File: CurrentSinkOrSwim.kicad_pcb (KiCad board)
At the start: 2 copper layers, 41.6 x 50.5 mm, 23 parts, among them P101 CONN_01X02, P102 CONN_01X03, P103 CONN_01X02, P201 CONN_01X01, Q201 BUK9575, U201 LMV358, U401 LM2931

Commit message: Lets try layout one more time. Starting layout from scratch
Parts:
- C201, C301, C401, C402: moved to F.Cu
- moved P101 74.4 mm to (184.3, 86.9), turned to 0 degrees
- moved C401 65.2 mm to (180.9, 111.4)
- moved R402 65.0 mm to (176.7, 111.4)
- moved C402 63.9 mm to (185.5, 105.2)
- moved R401 61.0 mm to (176.7, 105.2)
- moved RV301 59.0 mm to (106.1, 127.0), turned to 0 degrees
- moved P103 55.8 mm to (195.9, 86.9), turned to 0 degrees
- moved R403 54.3 mm to (181.1, 105.2)
- moved D301 52.7 mm to (117.9, 124.0), turned to 0 degrees
- moved P102 51.8 mm to (173.4, 85.4), turned to 0 degrees
- moved U401 51.0 mm to (171.5, 106.1), turned to 0 degrees
- moved R302 46.6 mm to (118.8, 132.0)
- moved Q201 45.8 mm to (123.3, 110.8)
- moved C301 45.7 mm to (114.5, 132.0)
- moved RV201 40.5 mm to (148.2, 87.0), turned to 0 degrees
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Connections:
- P102 pad 3: Net-(P102-Pad3) -> /Current Control/Current_Sink+
- P103 pad 1: Net-(P102-Pad3) -> /Current Control/Current_Sink+
- Q201 pad 1: /Current Control/Current_Sink+ -> /Current Control/FetGate
- Q201 pad 2: /Current Control/FetGate -> /Current Control/Current_Sink+
- R203 pad 2: /Current Control/Current_Sink- -> GND
- R302 pad 1: /Voltage Control/Current_Sink+ -> /Current Control/Current_Sink+
- RV201 pad 2: /Current Control/Current_Sink- -> GND
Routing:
- removed copper zone on B.Cu, net GND
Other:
- board outline removed
- rule pad_to_mask_clearance: 0.2 -> 0

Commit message: Intermediate layout version 2
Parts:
- C201, C301, C401, C402: moved to B.Cu
- moved R203 74.1 mm to (163.2, 68.8)
- moved D301 74.0 mm to (159.5, 62.8), turned to 180 degrees
- moved R302 72.3 mm to (152.1, 67.9), turned to 270 degrees
- moved Q201 65.0 mm to (159.5, 56.8)
- moved R301 60.5 mm to (145.3, 71.3), turned to 90 degrees
- moved RV301 58.9 mm to (142.2, 80.5), turned to 270 degrees
- moved C301 57.0 mm to (150.9, 88.1), turned to 270 degrees
- moved P201 55.1 mm to (159.5, 52.8)
- moved C201 52.4 mm to (169.6, 72.4)
- moved R303 50.6 mm to (152.3, 79.3), turned to 270 degrees
- moved P101 41.5 mm to (144.3, 98.2)
- moved R202 36.9 mm to (155.5, 69.7), turned to 270 degrees
- moved R401 32.5 mm to (152.9, 83.0), turned to 180 degrees
- moved RV201 29.4 mm to (176.9, 80.2), turned to 90 degrees
- moved R403 27.6 mm to (165.7, 82.2)
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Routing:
- net /Current Control/Current_Sink+: track 0.00 -> 72.4 mm
- net GND: track 0.00 -> 36.7 mm
- net Net-(Q201-Pad3): track 0.00 -> 28.0 mm
- net Net-(R201-Pad2): track 0.00 -> 18.9 mm
- net Net-(P101-Pad1): track 0.00 -> 17.1 mm
- net Net-(R302-Pad2): track 0.00 -> 15.7 mm
- net /Current Control/FetGate: track 0.00 -> 12.6 mm
- net /Power Regulation/Vin: track 0.00 -> 9.97 mm
- net Net-(R301-Pad2): track 0.00 -> 8.90 mm
- net Net-(R402-Pad2): track 0.00 -> 7.11 mm
- net 2.7V: track 0.00 -> 5.07 mm
- net Net-(R401-Pad1): track 0.00 -> 3.18 mm
- added copper zone on B.Cu, net GND
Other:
- board outline added: 41.6 x 61.3 mm
- net class Default: clearance 0.2 -> 0.254; trace_width 0.25 -> 0.254; via_dia 0.6 -> 0.889; via_drill 0.4 -> 0.635
- net class Power added: clearance 0.3048, trace_width 0.6096, via_dia 1.143, via_drill 0.762
- rule trace_clearance: 0.2 -> 0.254

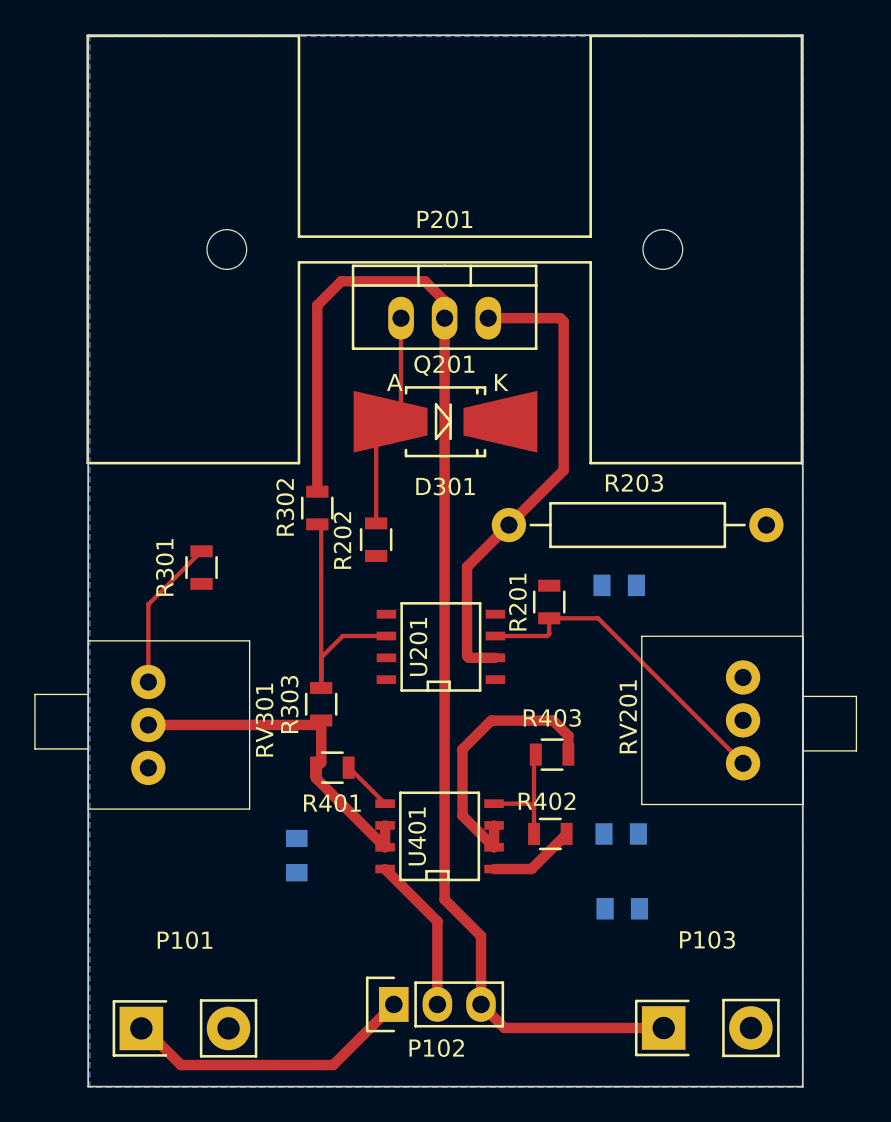
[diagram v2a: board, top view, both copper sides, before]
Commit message: A very compressed layout
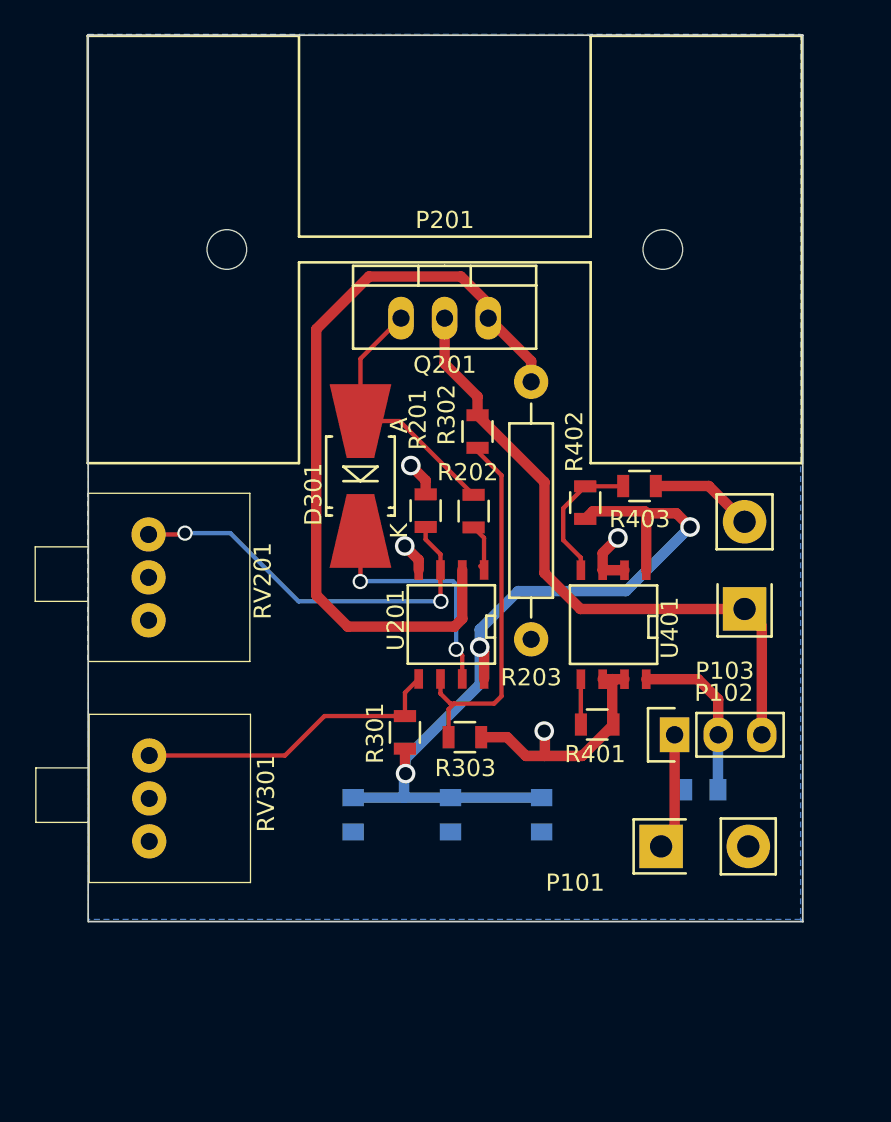
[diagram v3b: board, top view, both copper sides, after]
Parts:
- moved RV201 35.6 mm to (142.2, 71.9), turned to 270 degrees
- moved P101 32.1 mm to (174.6, 87.6)
- moved P103 27.0 mm to (176.9, 71.2), turned to 90 degrees
- moved P102 22.7 mm to (172.9, 81.1)
- moved C201 20.5 mm to (154.1, 85.7), turned to 270 degrees
- moved R402 19.4 mm to (167.7, 67.5), turned to 90 degrees
- moved R403 16.5 mm to (170.8, 66.6)
- moved U401 16.0 mm to (169.3, 74.7), turned to 180 degrees
- moved R401 15.6 mm to (168.4, 80.5), turned to 0 degrees
- moved R301 15.3 mm to (157.2, 80.9)
- moved C301 14.5 mm to (165.1, 85.7)
- moved R302 10.3 mm to (161.4, 63.4)
- moved C402 10.0 mm to (159.8, 85.7), turned to 270 degrees
- moved R201 8.95 mm to (158.4, 68.0)
- moved R303 8.59 mm to (160.7, 81.2), turned to 0 degrees
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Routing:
- net 2.7V: track 5.07 -> 52.8 mm, vias 0 -> 4
- net /Current Control/Current_Sink+: track 72.4 -> 37.5 mm
- net Net-(Q201-Pad3): track 28.0 -> 45.3 mm
- net Net-(D301-Pad1): track 0.00 -> 14.3 mm, vias 0 -> 2
- net GND: track 36.7 -> 25.6 mm, vias 0 -> 3
- net Net-(P101-Pad1): track 17.1 -> 6.83 mm
- net Net-(R301-Pad2): track 8.90 -> 18.3 mm
- net Net-(R302-Pad2): track 15.7 -> 22.0 mm
- net Net-(R201-Pad2): track 18.9 -> 23.5 mm, vias 0 -> 2
- net Net-(R202-Pad2): track 0.00 -> 3.05 mm
- net /Current Control/FetGate: track 12.6 -> 15.4 mm
- net Net-(R402-Pad2): track 7.11 -> 8.06 mm
- net Net-(R401-Pad1): track 3.18 -> 2.64 mm
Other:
- board size 41.6 x 61.3 mm -> 41.7 x 51.6 mm

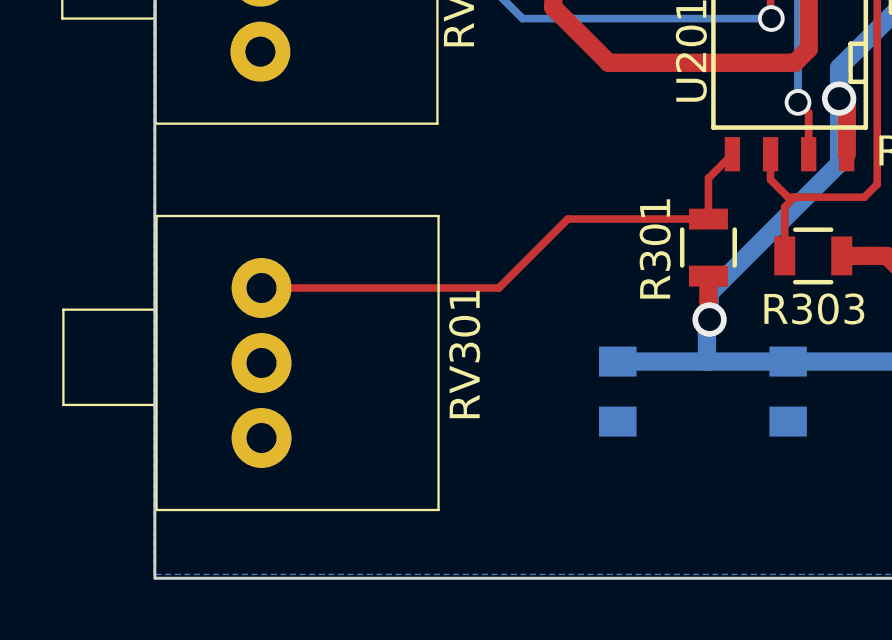
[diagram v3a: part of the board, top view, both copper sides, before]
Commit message: Minor adjustment to the pot position
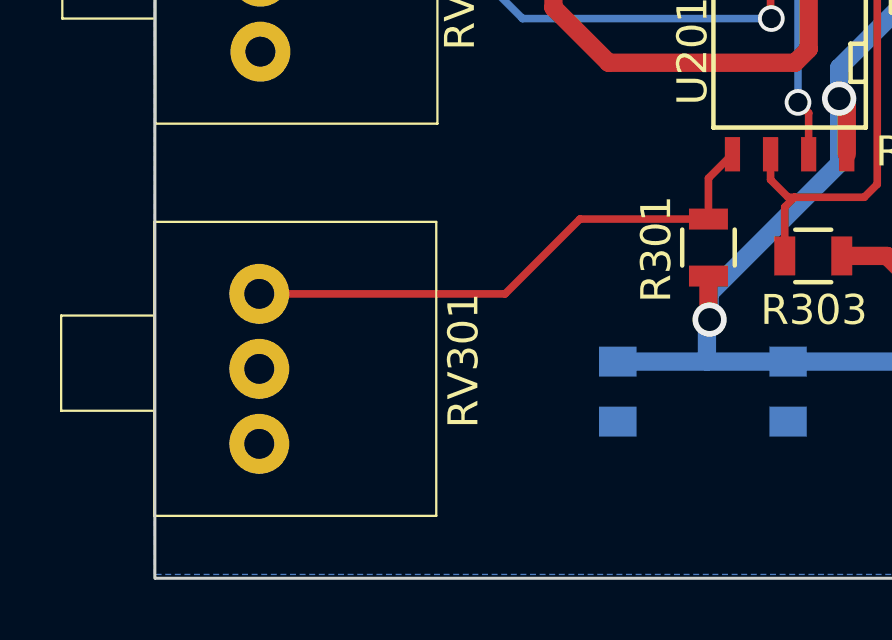
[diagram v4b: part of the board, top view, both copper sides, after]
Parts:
- moved RV301 0.21 mm to (142.2, 85.0)
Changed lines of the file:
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@@
   )
   (module current:P090L-02F25BR10K (layer F.Cu)
-    (at 142.2654 84.7725 270)
+    (at 142.1892 84.96808 270)
     (fp_text reference RV301 (at -0.2794 -6.8072 450) (layer F.SilkS)
       (effects (font (size 1 1) (thickness 0.15)))
@@
   (segment (start 172.8724 81.0641) (end 172.8724 86.7791) (width 0.6096) (layer F.Cu) (net 6))
   (segment (start 172.8724 86.7791) (end 172.085 87.5665) (width 0.6096) (layer F.Cu) (net 6))
-  (segment (start 161.3916 62.4484) (end 161.3916 61.3664) (width 0.6096) (layer F.Cu) (net 7) (status 400000))
-  (segment (start 159.4739 59.4487) (end 159.4739 56.7944) (width 0.6096) (layer F.Cu) (net 7) (status 800000))
+  (segment (start 161.3916 62.4484) (end 161.3916 61.3664) (width 0.6096) (layer F.Cu) (net 7))
+  (segment (start 159.4739 59.4487) (end 159.4739 56.7944) (width 0.6096) (layer F.Cu) (net 7))
   (segment (start 161.3916 61.3664) (end 159.4739 59.4487) (width 0.6096) (layer F.Cu) (net 7))
-  (segment (start 176.9491 73.7362) (end 167.386 73.7362) (width 0.6096) (layer F.Cu) (net 7) (status 400000))
-  (segment (start 165.2905 66.3473) (end 161.3916 62.4484) (width 0.6096) (layer F.Cu) (net 7) (status 800000))
+  (segment (start 176.9491 73.7362) (end 167.386 73.7362) (width 0.6096) (layer F.Cu) (net 7))
+  (segment (start 165.2905 66.3473) (end 161.3916 62.4484) (width 0.6096) (layer F.Cu) (net 7))
   (segment (start 165.2905 71.6407) (end 165.2905 66.3473) (width 0.6096) (layer F.Cu) (net 7))
   (segment (start 167.386 73.7362) (end 165.2905 71.6407) (width 0.6096) (layer F.Cu) (net 7))
@@
   (segment (start 161.7726 69.5935) (end 161.163 68.9839) (width 0.254) (layer F.Cu) (net 10))
   (segment (start 161.544 71.2343) (end 161.7726 71.4629) (width 0.254) (layer F.Cu) (net 10))
-  (segment (start 157.1625 79.9744) (end 152.4737 79.9744) (width 0.254) (layer F.Cu) (net 11))
-  (segment (start 150.1756 82.2725) (end 142.2654 82.2725) (width 0.254) (layer F.Cu) (net 11))
-  (segment (start 152.4737 79.9744) (end 150.1756 82.2725) (width 0.254) (layer F.Cu) (net 11))
+  (segment (start 157.1625 79.9744) (end 152.87756 79.9744) (width 0.254) (layer F.Cu) (net 11) (status 400000))
+  (segment (start 150.38388 82.46808) (end 142.1892 82.46808) (width 0.254) (layer F.Cu) (net 11) (status 800000))
+  (segment (start 152.87756 79.9744) (end 150.38388 82.46808) (width 0.254) (layer F.Cu) (net 11))
   (segment (start 157.1625 79.9744) (end 157.1625 78.613) (width 0.254) (layer F.Cu) (net 11))
   (segment (start 157.1625 78.613) (end 157.9626 77.8129) (width 0.254) (layer F.Cu) (net 11))

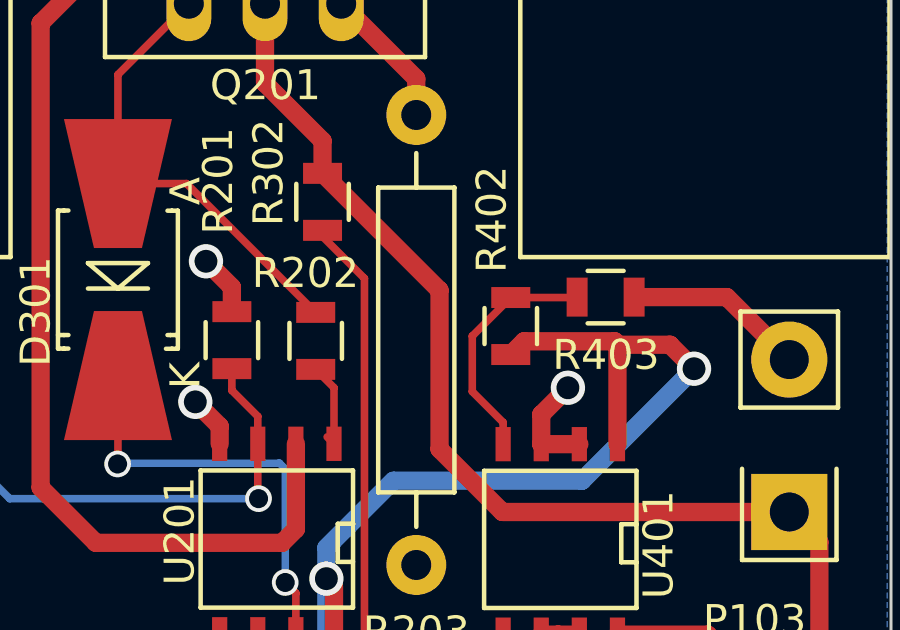
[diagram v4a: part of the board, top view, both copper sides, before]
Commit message: Found a missed 2.7 connection
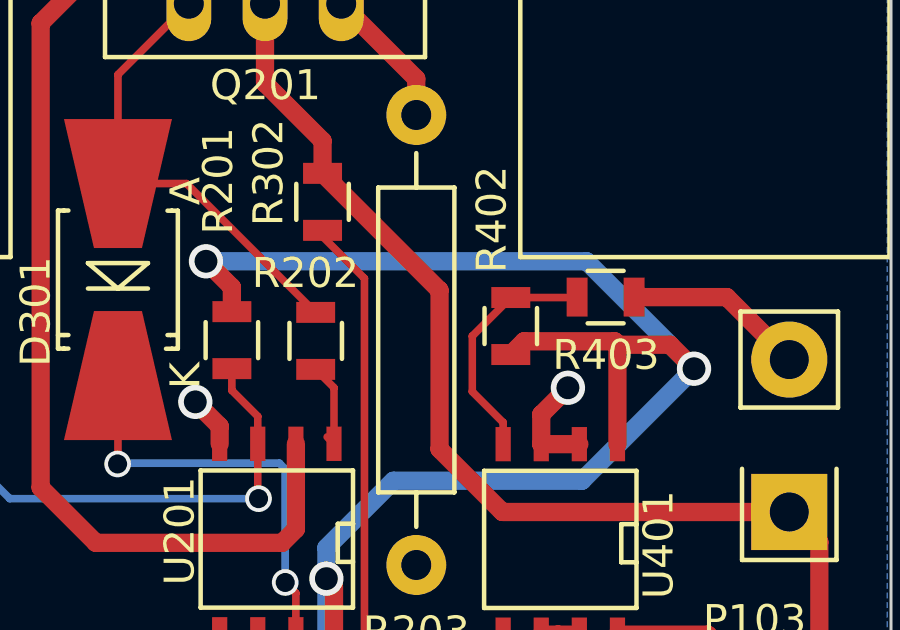
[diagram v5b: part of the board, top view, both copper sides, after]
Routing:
- net 2.7V: track 52.8 -> 70.6 mm
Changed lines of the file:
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@@
   (general
     (links 44)
-    (no_connects 12)
+    (no_connects 0)
     (area 135.267699 39.968099 183.807101 101.922901)
     (thickness 1.6)
     (drawings 4)
-    (tracks 134)
+    (tracks 136)
     (zones 0)
     (modules 23)
@@
   (gr_line (start 138.7348 91.948) (end 180.3654 91.948) (angle 90) (layer Edge.Cuts) (width 0.1))
   (gr_line (start 138.7094 40.3098) (end 138.7094 91.948) (angle 90) (layer Edge.Cuts) (width 0.1))
+  (segment (start 157.5054 65.3796) (end 170.1927 65.3796) (width 0.6096) (layer B.Cu) (net 1))
+  (segment (start 158.369 66.2432) (end 157.5054 65.3796) (width 0.6096) (layer F.Cu) (net 1))
+  (via (at 157.5054 65.3796) (size 1.143) (drill 0.762) (layers F.Cu B.Cu) (net 1))
+  (segment (start 158.369 67.0585) (end 158.369 66.2432) (width 0.6096) (layer F.Cu) (net 1))
+  (segment (start 170.1927 65.3796) (end 173.7741 68.961) (width 0.6096) (layer B.Cu) (net 1))
   (segment (start 157.1117 84.725) (end 157.1117 83.4136) (width 0.6096) (layer B.Cu) (net 1))
   (segment (start 157.1117 83.4136) (end 157.2006 83.3247) (width 0.6096) (layer B.Cu) (net 1))
@@
   (via (at 161.5186 75.9587) (size 1.143) (drill 0.762) (layers F.Cu B.Cu) (net 1))
   (segment (start 161.7726 76.2127) (end 161.7726 77.8129) (width 0.6096) (layer F.Cu) (net 1))
-  (segment (start 158.369 67.0585) (end 158.369 66.2432) (width 0.6096) (layer F.Cu) (net 1))
-  (via (at 157.5054 65.3796) (size 1.143) (drill 0.762) (layers F.Cu B.Cu) (net 1))
-  (segment (start 158.369 66.2432) (end 157.5054 65.3796) (width 0.6096) (layer F.Cu) (net 1))
   (segment (start 157.1625 81.8744) (end 157.1625 83.2866) (width 0.6096) (layer F.Cu) (net 1))
   (segment (start 157.1625 83.2866) (end 157.2006 83.3247) (width 0.6096) (layer F.Cu) (net 1))
@@
   (segment (start 177.9524 81.0641) (end 177.9524 74.7395) (width 0.6096) (layer F.Cu) (net 7))
   (segment (start 177.9524 74.7395) (end 176.9491 73.7362) (width 0.6096) (layer F.Cu) (net 7))
+  (segment (start 162.0139 55.9562) (end 160.4264 54.3687) (width 0.6096) (layer F.Cu) (net 8))
+  (segment (start 160.4264 54.3687) (end 155.067 54.3687) (width 0.6096) (layer F.Cu) (net 8))
+  (segment (start 155.067 54.3687) (end 151.9936 57.4421) (width 0.6096) (layer F.Cu) (net 8))
+  (segment (start 151.9936 57.4421) (end 151.9936 72.9234) (width 0.6096) (layer F.Cu) (net 8))
+  (segment (start 151.9936 72.9234) (end 153.8351 74.7649) (width 0.6096) (layer F.Cu) (net 8))
+  (segment (start 153.8351 74.7649) (end 160.0454 74.7649) (width 0.6096) (layer F.Cu) (net 8))
+  (segment (start 160.0454 74.7649) (end 160.5026 74.3077) (width 0.6096) (layer F.Cu) (net 8))
+  (segment (start 160.5026 74.3077) (end 160.5026 71.4629) (width 0.6096) (layer F.Cu) (net 8))
   (segment (start 162.0139 56.7944) (end 162.0139 55.9562) (width 0.6096) (layer F.Cu) (net 8))
-  (segment (start 162.0139 55.9562) (end 160.4264 54.3687) (width 0.6096) (layer F.Cu) (net 8))
-  (segment (start 160.5026 74.3077) (end 160.5026 71.4629) (width 0.6096) (layer F.Cu) (net 8))
-  (segment (start 160.0454 74.7649) (end 160.5026 74.3077) (width 0.6096) (layer F.Cu) (net 8))
-  (segment (start 153.8351 74.7649) (end 160.0454 74.7649) (width 0.6096) (layer F.Cu) (net 8))
-  (segment (start 151.9936 72.9234) (end 153.8351 74.7649) (width 0.6096) (layer F.Cu) (net 8))
-  (segment (start 151.9936 57.4421) (end 151.9936 72.9234) (width 0.6096) (layer F.Cu) (net 8))
-  (segment (start 155.067 54.3687) (end 151.9936 57.4421) (width 0.6096) (layer F.Cu) (net 8))
-  (segment (start 160.4264 54.3687) (end 155.067 54.3687) (width 0.6096) (layer F.Cu) (net 8))
   (segment (start 164.5158 60.5028) (end 164.5158 59.2963) (width 0.6096) (layer F.Cu) (net 8))
   (segment (start 164.5158 59.2963) (end 162.0139 56.7944) (width 0.6096) (layer F.Cu) (net 8))
@@
   (segment (start 161.7726 69.5935) (end 161.163 68.9839) (width 0.254) (layer F.Cu) (net 10))
   (segment (start 161.544 71.2343) (end 161.7726 71.4629) (width 0.254) (layer F.Cu) (net 10))
-  (segment (start 157.1625 79.9744) (end 152.87756 79.9744) (width 0.254) (layer F.Cu) (net 11) (status 400000))
-  (segment (start 150.38388 82.46808) (end 142.1892 82.46808) (width 0.254) (layer F.Cu) (net 11) (status 800000))
+  (segment (start 157.1625 79.9744) (end 152.87756 79.9744) (width 0.254) (layer F.Cu) (net 11))
+  (segment (start 150.38388 82.46808) (end 142.1892 82.46808) (width 0.254) (layer F.Cu) (net 11))
   (segment (start 152.87756 79.9744) (end 150.38388 82.46808) (width 0.254) (layer F.Cu) (net 11))
   (segment (start 157.1625 79.9744) (end 157.1625 78.613) (width 0.254) (layer F.Cu) (net 11))
@@
     (connect_pads (clearance 0.508))
     (min_thickness 0.254)
-    (fill (arc_segments 16) (thermal_gap 0.508) (thermal_bridge_width 0.508))
+    (fill yes (arc_segments 16) (thermal_gap 0.508) (thermal_bridge_width 0.508))
     (polygon
       (pts
@@
     (connect_pads (clearance 0.508))
     (min_thickness 0.254)
-    (fill (arc_segments 16) (thermal_gap 0.508) (thermal_bridge_width 0.508))
+    (fill yes (arc_segments 16) (thermal_gap 0.508) (thermal_bridge_width 0.508))
     (polygon
       (pts
